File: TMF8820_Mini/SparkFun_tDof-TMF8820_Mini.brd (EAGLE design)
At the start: 25.4 x 12.7 mm, 53 parts, among them J4 QWIIC_RIGHT_ANGLE, J5 QWIIC_RIGHT_ANGLE

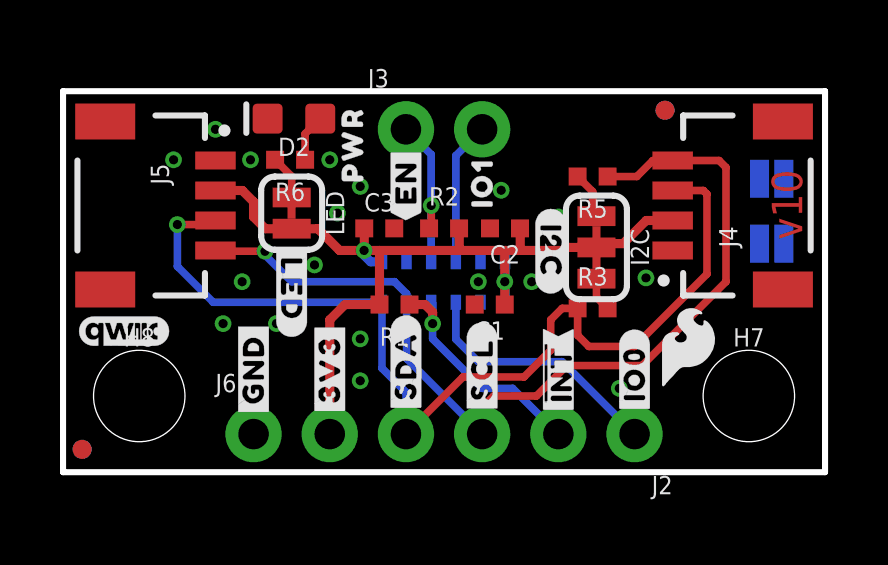
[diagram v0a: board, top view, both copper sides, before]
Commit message: Removes old production files
* Removes old 8821 "HQ" variants
* Copies the 8820 and 8820 Mini variants
* Adjusts new 8820 copies to reference 8821 and replaces 8820 with 8821
* Updates Product Identifier jumpers to reflect changes
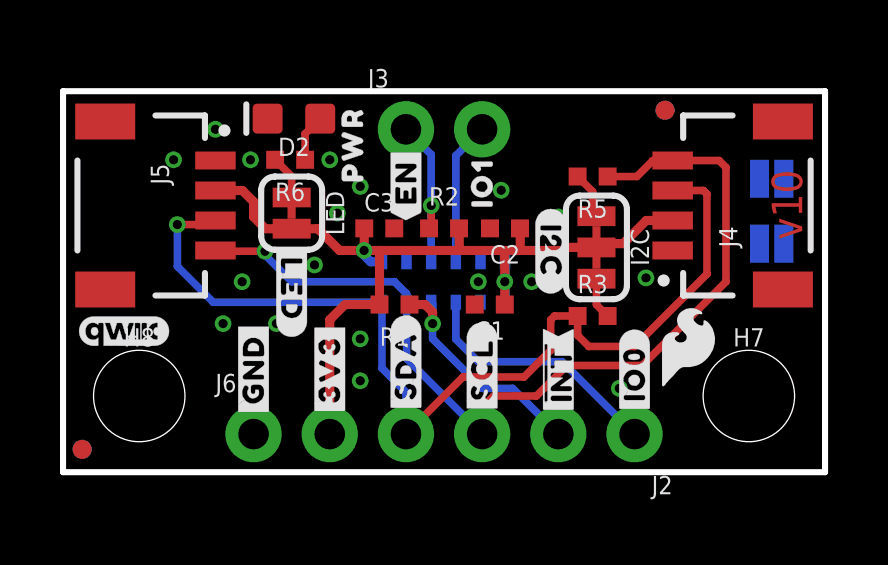
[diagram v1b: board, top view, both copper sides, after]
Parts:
- moved R3 0.25 mm to (17.7, 5.21)
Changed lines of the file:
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@@
 <attribute name="VALUE" x="5.08" y="-0.762" size="0.6096" layer="27" font="vector" ratio="20"/>
 </element>
-<element name="R3" library="SparkFun-Resistors" package="0402-TIGHT" value="2.2k" x="17.653" y="5.461" smashed="yes">
-<attribute name="NAME" x="17.653" y="6.223" size="0.6096" layer="25" font="vector" ratio="20" align="bottom-center"/>
-<attribute name="PROD_ID" value="RES-14341" x="17.653" y="5.461" size="1.778" layer="27" display="off"/>
-<attribute name="VALUE" value="2.2k" x="17.653" y="4.699" size="0.6096" layer="27" font="vector" ratio="20" align="top-center"/>
+<element name="R3" library="SparkFun-Resistors" package="0402-TIGHT" value="2.2k" x="17.653" y="5.207" smashed="yes">
+<attribute name="NAME" x="17.653" y="5.969" size="0.6096" layer="25" font="vector" ratio="20" align="bottom-center"/>
+<attribute name="PROD_ID" value="RES-14341" x="17.653" y="5.207" size="1.778" layer="27" display="off"/>
+<attribute name="VALUE" value="2.2k" x="17.653" y="4.445" size="0.6096" layer="27" font="vector" ratio="20" align="top-center"/>
 </element>
 <element name="R5" library="SparkFun-Resistors" package="0402-TIGHT" value="2.2k" x="17.653" y="9.8552" smashed="yes" rot="R180">
@@
 <wire x1="21.344" y1="9.39" x2="21.463" y2="9.271" width="0.254" layer="1"/>
 <wire x1="21.463" y1="9.271" x2="21.463" y2="6.604" width="0.254" layer="1"/>
-<wire x1="17.153" y1="4.564" x2="17.153" y2="5.461" width="0.254" layer="1"/>
+<wire x1="17.153" y1="4.564" x2="17.153" y2="5.207" width="0.254" layer="1"/>
 <wire x1="21.463" y1="6.604" x2="19.05" y2="4.191" width="0.254" layer="1"/>
 <wire x1="19.05" y1="4.191" x2="17.526" y2="4.191" width="0.254" layer="1"/>
 <wire x1="17.526" y1="4.191" x2="17.153" y2="4.564" width="0.254" layer="1"/>
-<wire x1="17.153" y1="5.461" x2="16.637" y2="5.461" width="0.254" layer="1"/>
-<wire x1="16.256" y1="5.08" x2="16.637" y2="5.461" width="0.254" layer="1"/>
 <wire x1="15.367" y1="3.175" x2="13.335" y2="3.175" width="0.254" layer="1"/>
 <wire x1="13.335" y1="3.175" x2="11.43" y2="1.27" width="0.254" layer="1"/>
@@
 <wire x1="16.256" y1="4.064" x2="16.256" y2="5.08" width="0.254" layer="1"/>
 <wire x1="15.367" y1="3.175" x2="16.256" y2="4.064" width="0.254" layer="1"/>
+<wire x1="16.256" y1="5.08" x2="16.383" y2="5.207" width="0.254" layer="1"/>
+<wire x1="16.383" y1="5.207" x2="17.153" y2="5.207" width="0.254" layer="1"/>
 </signal>
 <signal name="N$5">
@@
 <contactref element="R3" pad="2"/>
 <contactref element="I2C" pad="3"/>
-<wire x1="18.153" y1="5.461" x2="17.78" y2="5.834" width="0.254" layer="1"/>
-<wire x1="17.78" y1="5.834" x2="17.78" y2="6.4516" width="0.254" layer="1"/>
+<wire x1="18.153" y1="5.207" x2="17.78" y2="5.58" width="0.254" layer="1"/>
+<wire x1="17.78" y1="5.58" x2="17.78" y2="6.4516" width="0.254" layer="1"/>
 </signal>
 <signal name="N$8">

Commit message: Adds new product identifier pads to all designs, rolls 8820 version number to v10
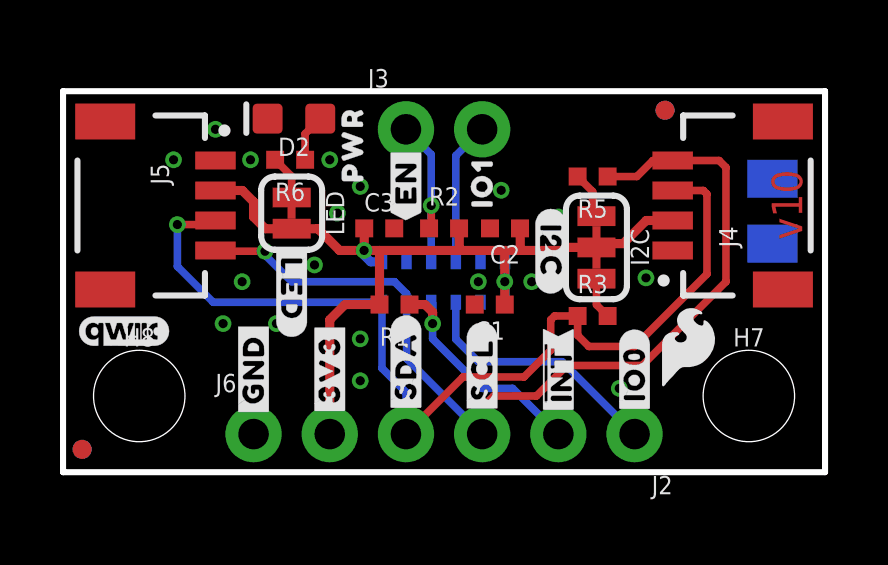
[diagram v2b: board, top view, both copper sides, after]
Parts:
- TMF8820: value JUMPER-SMT_2_NC_PASTE_SILK -> PROD_ID_PASTE_SILK; device SparkFun-Jumpers:SMT-JUMPER_2_NC_PASTE_SILK -> SparkFun-Aesthetics:PRODUCT_IDENT_PASTE_SILK
- TMF8821: value JUMPER-SMT_2_NO_SILK -> PROD_ID_NO-PASTE_SILK; device SparkFun-Jumpers:SMT-JUMPER_2_NO_SILK -> SparkFun-Aesthetics:PRODUCT_IDENT_NO_SILK
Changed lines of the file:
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@@
 <drawing>
 <settings>
-<setting alwaysvectorfont="yes"/>
+<setting alwaysvectorfont="no"/>
 <setting verticaltext="up"/>
 </settings>
@@
 <layer number="115" name="ReferenceISLANDS" color="7" fill="1" visible="no" active="no"/>
 <layer number="116" name="Patch_BOT" color="9" fill="4" visible="no" active="no"/>
-<layer number="117" name="PM_Ref" color="26" fill="1" visible="no" active="yes"/>
+<layer number="117" name="PM_Ref" color="26" fill="1" visible="yes" active="yes"/>
 <layer number="118" name="Rect_Pads" color="7" fill="1" visible="no" active="no"/>
-<layer number="119" name="PF_Ref" color="31" fill="1" visible="no" active="yes"/>
-<layer number="120" name="WFL_Ref" color="25" fill="1" visible="no" active="yes"/>
+<layer number="119" name="PF_Ref" color="31" fill="1" visible="yes" active="yes"/>
+<layer number="120" name="WFL_Ref" color="25" fill="1" visible="yes" active="yes"/>
 <layer number="121" name="_tsilk" color="7" fill="1" visible="no" active="no"/>
 <layer number="122" name="_bsilk" color="7" fill="1" visible="no" active="no"/>
@@
 <element name="LOGO3" library="SparkFun-Aesthetics" package="DUMMY" value="OSHW-LOGONO_SILK" x="-11.938" y="-12.954" smashed="yes"/>
 <element name="U$2" library="TMFHQTopSilk" package="#IO0#8" value="" x="19.05" y="3.302" smashed="yes" rot="R90"/>
-<element name="TMF8820" library="SparkFun-Jumpers" package="SMT-JUMPER_2_NC_PASTE_SILK" package3d_urn="urn:adsk.eagle:package:39282/1" value="JUMPER-SMT_2_NC_PASTE_SILK" x="23.622" y="9.779" smashed="yes" rot="MR0">
+<element name="TMF8820" library="SparkFun-Aesthetics" package="PRODUCT_IDENT_PASTE_SILK" value="PROD_ID_PASTE_SILK" x="23.622" y="9.779" smashed="yes" rot="MR0">
 <attribute name="NAME" x="23.622" y="10.922" size="0.6096" layer="26" font="vector" ratio="20" rot="MR0" align="bottom-center"/>
 <attribute name="VALUE" x="23.622" y="8.636" size="0.6096" layer="28" font="vector" ratio="20" rot="MR0" align="top-center"/>
 </element>
-<element name="TMF8821" library="SparkFun-Jumpers" package="SMT-JUMPER_2_NO_SILK" package3d_urn="urn:adsk.eagle:package:39279/1" value="JUMPER-SMT_2_NO_SILK" x="23.622" y="7.62" smashed="yes" rot="MR0">
+<element name="TMF8821" library="SparkFun-Aesthetics" package="PRODUCT_IDENT_NO_SILK" value="PROD_ID_NO-PASTE_SILK" x="23.622" y="7.62" smashed="yes" rot="MR0">
 <attribute name="NAME" x="23.622" y="8.763" size="0.6096" layer="26" font="vector" ratio="20" rot="MR0" align="bottom-center"/>
 <attribute name="VALUE" x="23.622" y="6.477" size="0.6096" layer="28" font="vector" ratio="20" rot="MR0" align="top-center"/>

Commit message: Changes all "IO" silk to be "GP" instead, increases Qwiic pill size on mini's
* Fixes orientation of I2C and LED silk on mini versions
* Increases SparkFun flame size on mini versions
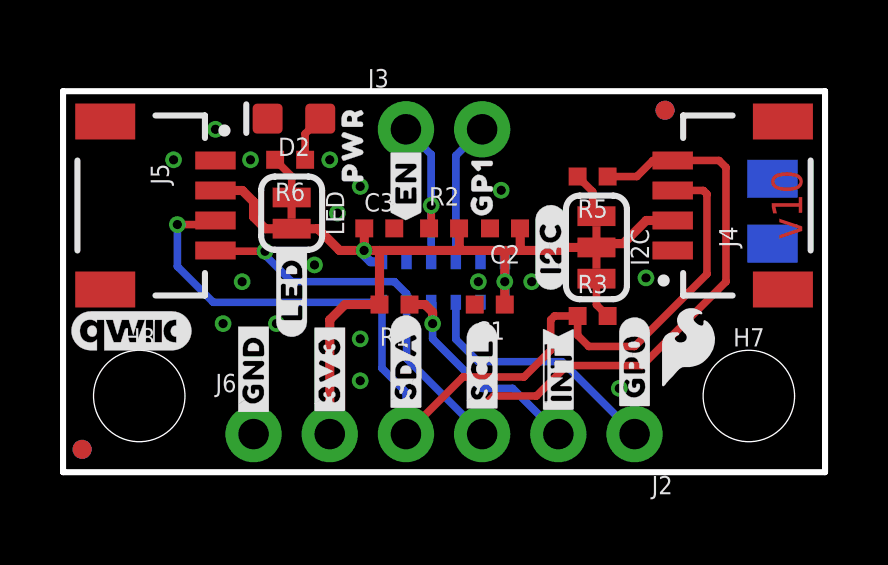
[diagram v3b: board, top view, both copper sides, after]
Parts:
- removed U$22: (no value), TMFHQBotSilk:#LED#10
- removed U$33: (no value), SparkFun-Aesthetics:SFE_LOGO_FLAME_.1
- added U$13: (no value), TMFMiniBotSilk:#LED#10
- added U$14: (no value), TMFMiniTop:#GP0#19
- LOGO2: value QWIIC_LOGO_3MM -> QWIIC_LOGO_4MM; device SparkFun-Aesthetics:QWIIC_3MM -> SparkFun-Aesthetics:QWIIC_4MM
- U$12: device TMFMiniTop:IO18 -> SparkFun-Aesthetics:SFE_LOGO_FLAME_.2
- U$2: device TMFHQTopSilk:#IO0#8 -> TMFMiniBotSilk:#GP1#8
- U$6: device TMFHQTopSilk:#IO1#8 -> TMFMiniTop:GP18
- moved U$12 11.5 mm to (2.54, 8.89), flipped to the bottom, turned to 0 degrees
- moved U$2 7.94 mm to (14.0, 9.40), flipped to the bottom, turned to 270 degrees
- moved LOGO2 0.25 mm to (2.29, 4.70)
- moved U$20 0.13 mm to (16.3, 7.49), turned to 90 degrees
- flipped U$6 to the top, turned to 90 degrees
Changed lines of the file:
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@@
 <element name="U$18" library="TMFHQBotSilk" package="#SDA#6" value="" x="11.43" y="3.556" smashed="yes" rot="MR270"/>
 <element name="U$19" library="TMFHQBotSilk" package="#SCL#5" value="" x="13.97" y="3.429" smashed="yes" rot="MR270"/>
-<element name="U$20" library="TMFHQBotSilk" package="#I2C#11" value="" x="16.256" y="7.366" smashed="yes" rot="R270"/>
-<element name="U$22" library="TMFHQBotSilk" package="#LED#10" value="" x="7.62" y="6.096" smashed="yes" rot="R270"/>
-<element name="U$33" library="SparkFun-Aesthetics" package="SFE_LOGO_FLAME_.1" value="" x="2.159" y="8.763" smashed="yes" rot="MR0"/>
+<element name="U$20" library="TMFHQBotSilk" package="#I2C#11" value="" x="16.256" y="7.493" smashed="yes" rot="R90"/>
 <element name="U$35" library="SparkFun-Aesthetics" package="SFE_LOGO_FLAME_.1" value="" x="20.828" y="4.191" smashed="yes"/>
 <element name="U$37" library="TMFHQTopSilk" package="#3V3#0" value="" x="8.89" y="3.429" smashed="yes" rot="R90"/>
@@
 <element name="U$4" library="TMFHQTopSilk" package="##INT##8" value="" x="16.51" y="3.302" smashed="yes" rot="MR270"/>
 <element name="U$5" library="TMFHQBotSilk" package="#SYNC#8" value="" x="19.05" y="3.937" smashed="yes" rot="MR270"/>
-<element name="U$6" library="TMFHQTopSilk" package="#IO1#8" value="" x="13.97" y="9.525" smashed="yes" rot="MR270"/>
 <element name="U$7" library="TMFHQTopSilk" package="DTOF882188211" value="" x="18.923" y="11.176" smashed="yes" rot="MR0"/>
 <element name="U$8" library="TMFHQTopSilk" package="TMF88209" value="" x="18.796" y="9.779" smashed="yes" rot="MR0"/>
 <element name="LOGO1" library="SparkFun-Aesthetics" package="BLANK" value="SFE_LOGO_NAMEBLANK" x="-11.938" y="-12.954" smashed="yes"/>
-<element name="LOGO2" library="SparkFun-Aesthetics" package="QWIIC_3MM" value="QWIIC_LOGO_3MM" x="2.032" y="4.699" smashed="yes"/>
+<element name="LOGO2" library="SparkFun-Aesthetics" package="QWIIC_4MM" value="QWIIC_LOGO_4MM" x="2.286" y="4.699" smashed="yes"/>
 <element name="LOGO3" library="SparkFun-Aesthetics" package="DUMMY" value="OSHW-LOGONO_SILK" x="-11.938" y="-12.954" smashed="yes"/>
-<element name="U$2" library="TMFHQTopSilk" package="#IO0#8" value="" x="19.05" y="3.302" smashed="yes" rot="R90"/>
 <element name="TMF8820" library="SparkFun-Aesthetics" package="PRODUCT_IDENT_PASTE_SILK" value="PROD_ID_PASTE_SILK" x="23.622" y="9.779" smashed="yes" rot="MR0">
 <attribute name="NAME" x="23.622" y="10.922" size="0.6096" layer="26" font="vector" ratio="20" rot="MR0" align="bottom-center"/>
@@
 <element name="U$9" library="TMFHQTopSilk" package="#EN#7" value="" x="11.43" y="9.652" smashed="yes" rot="R90"/>
 <element name="U$11" library="TMFHQTopSilk" package="TMF882188210" value="" x="18.923" y="7.62" smashed="yes" rot="MR0"/>
-<element name="U$12" library="TMFMiniTop" package="IO18" value="" x="13.97" y="9.652" smashed="yes" rot="R90"/>
+<element name="U$13" library="TMFMiniBotSilk" package="#LED#10" value="" x="7.62" y="6.096" smashed="yes" rot="R90"/>
+<element name="U$14" library="TMFMiniTop" package="#GP0#19" value="" x="19.05" y="3.556" smashed="yes" rot="R90"/>
+<element name="U$2" library="TMFMiniBotSilk" package="#GP1#8" value="" x="13.97" y="9.398" smashed="yes" rot="MR270"/>
+<element name="U$6" library="TMFMiniTop" package="GP18" value="" x="13.97" y="9.525" smashed="yes" rot="R90"/>
+<element name="U$12" library="SparkFun-Aesthetics" package="SFE_LOGO_FLAME_.2" value="" x="2.54" y="8.89" smashed="yes" rot="MR0"/>
 </elements>
 <signals>

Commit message: Adds OSHW logo to boards, fixes silk width of new product identifier pads
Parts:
- added U$15: (no value), SparkFun-Aesthetics:OSHW-LOGO-MINI
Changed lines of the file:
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@@
 <drawing>
 <settings>
-<setting alwaysvectorfont="no"/>
+<setting alwaysvectorfont="yes"/>
 <setting verticaltext="up"/>
 </settings>
@@
 <element name="U$6" library="TMFMiniTop" package="GP18" value="" x="13.97" y="9.525" smashed="yes" rot="R90"/>
 <element name="U$12" library="SparkFun-Aesthetics" package="SFE_LOGO_FLAME_.2" value="" x="2.54" y="8.89" smashed="yes" rot="MR0"/>
+<element name="U$15" library="SparkFun-Aesthetics" package="OSHW-LOGO-MINI" value="" x="2.413" y="5.715" smashed="yes" rot="MR0"/>
 </elements>
 <signals>
